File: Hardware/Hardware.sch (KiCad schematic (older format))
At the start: 18 parts, among them J1 Conn_01x02, J2 Conn_01x04, J4 Conn_01x02, J5 Conn_01x06, J6 Conn_01x08, J7 Conn_01x03, U1 ESP32-WROOM-32

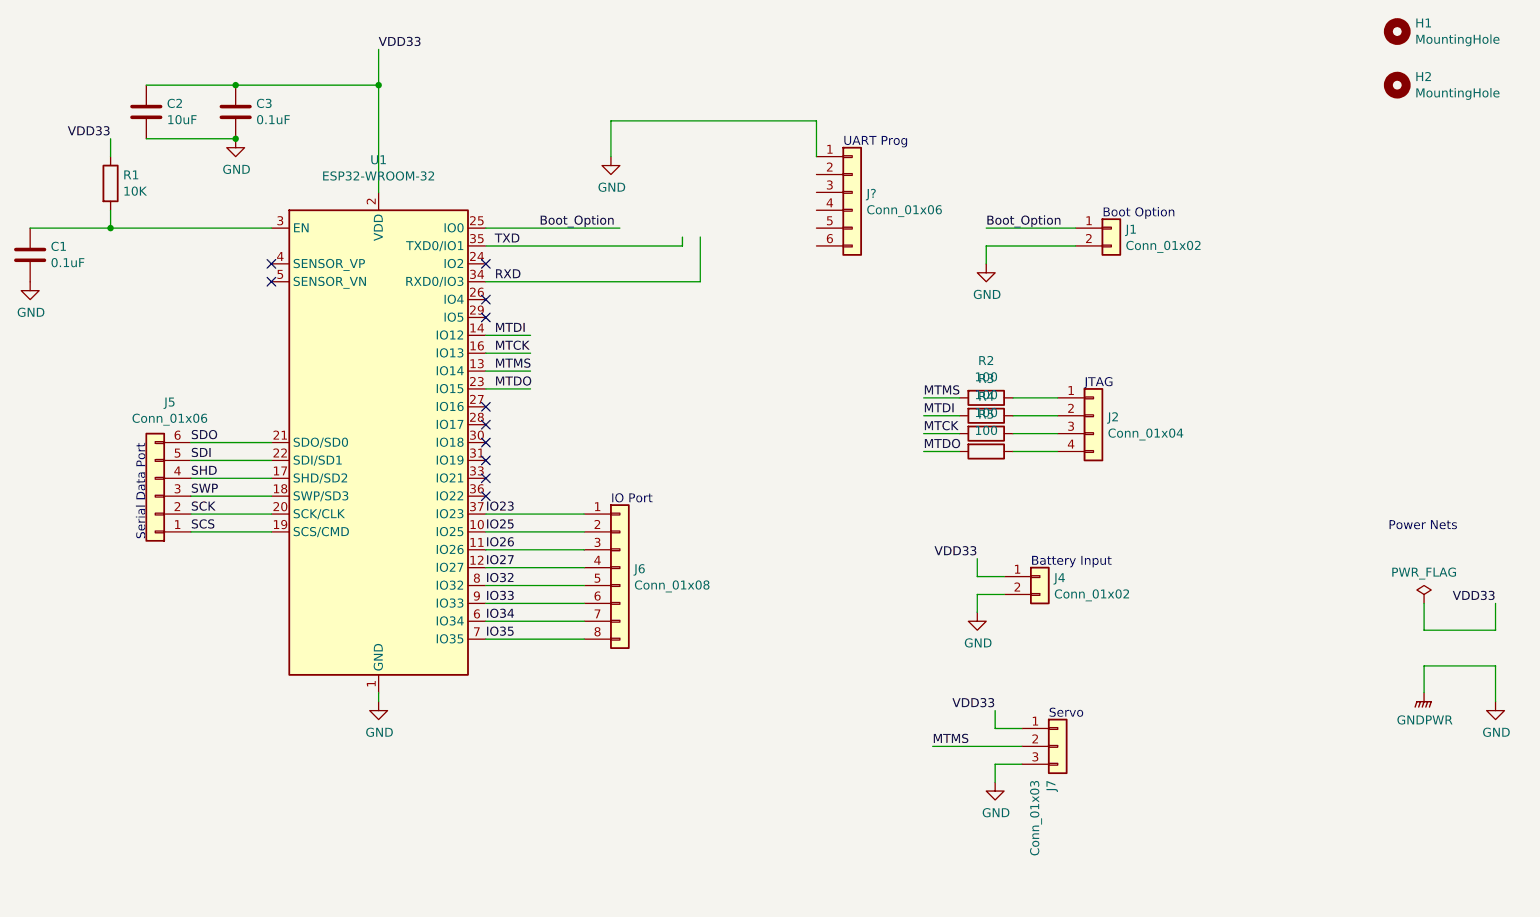
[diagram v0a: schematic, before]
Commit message: Programmer fix
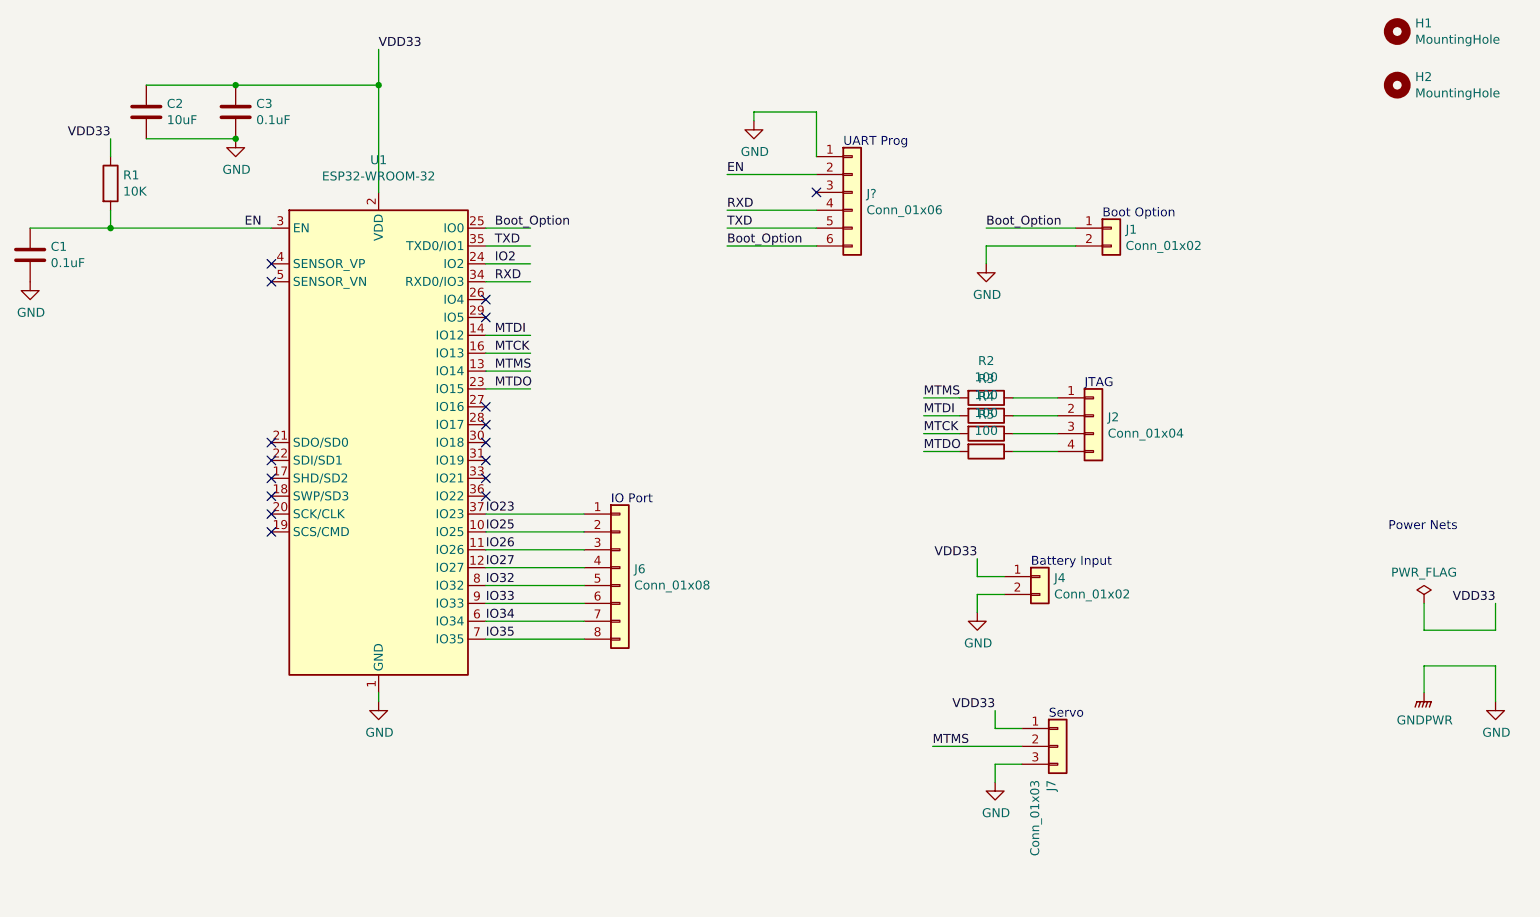
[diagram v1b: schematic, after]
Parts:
- removed J5: Conn_01x06, Connector_PinHeader_2.54mm:PinHeader_1x06_P2.54mm_Vertical, symbol Connector_Generic:Conn_01x06
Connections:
- net labels added: EN, IO2
- net labels removed: SCK, SCS, SDI, SDO, SHD, SWP
- wire segments 62 -> 59
- no-connect marks 11 -> 17
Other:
- note removed: "Serial Data Port"
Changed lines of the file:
@@
 	1    0    0    -1
 $EndComp
-Wire Wire Line
-	3200 2500 3950 2500
-Text Label 3500 2500 0    50   ~ 0
+Text Label 3250 2500 0    50   ~ 0
 Boot_Option
 $Comp
@@
 Wire Wire Line
 	6000 2600 6500 2600
-Wire Wire Line
-	3200 2600 4300 2600
-Wire Wire Line
-	4300 2600 4300 2550
-Wire Wire Line
-	4400 2550 4400 2800
-Wire Wire Line
-	4400 2800 3200 2800
-Text Notes 5200 2050 0    50   ~ 0
-UART Prog
 Text Label 3250 2600 0    50   ~ 0
 TXD
@@
 Text Label 3200 4800 0    50   ~ 0
 IO35
-$Comp
-L Connector_Generic:Conn_01x06 J5
-U 1 1 620D7FA6
-P 1350 4000
-F 0 "J5" H 1268 3475 50  0000 C CNN
-F 1 "Conn_01x06" H 1268 3566 50  0000 C CNN
-F 2 "Connector_PinHeader_2.54mm:PinHeader_1x06_P2.54mm_Vertical" H 1350 4000 50  0001 C CNN
-F 3 "~" H 1350 4000 50  0001 C CNN
-	1    1350 4000
-	-1   0    0    1
-$EndComp
-Wire Wire Line
-	2000 3800 1550 3800
-Wire Wire Line
-	1550 3900 2000 3900
-Wire Wire Line
-	1550 4000 2000 4000
-Wire Wire Line
-	1550 4100 2000 4100
-Wire Wire Line
-	2000 4200 1550 4200
-Wire Wire Line
-	1550 3700 2000 3700
-Text Label 1550 3700 0    50   ~ 0
-SDO
-Text Label 1550 3800 0    50   ~ 0
-SDI
-Text Label 1550 3900 0    50   ~ 0
-SHD
-Text Label 1550 4000 0    50   ~ 0
-SWP
-Text Label 1550 4100 0    50   ~ 0
-SCK
-Text Label 1550 4200 0    50   ~ 0
-SCS
-Text Notes 1300 4250 1    50   ~ 0
-Serial Data Port
-NoConn ~ 3200 2700
 NoConn ~ 3200 2900
 NoConn ~ 3200 3000
@@
 $EndComp
 $Comp
-L power:GND #PWR?
-U 1 1 6260035B
-P 3900 2100
-F 0 "#PWR?" H 3900 1850 50  0001 C CNN
-F 1 "GND" H 3905 1927 50  0000 C CNN
-F 2 "" H 3900 2100 50  0001 C CNN
-F 3 "" H 3900 2100 50  0001 C CNN
-	1    3900 2100
-	1    0    0    -1
-$EndComp
-Wire Wire Line
-	3900 2100 3900 1900
-Wire Wire Line
-	3900 1900 5050 1900
-Wire Wire Line
-	5050 1900 5050 2100
+L power:GND #PWR0105
+U 1 1 6209A315
+P 4700 1900
+F 0 "#PWR0105" H 4700 1650 50  0001 C CNN
+F 1 "GND" H 4705 1727 50  0000 C CNN
+F 2 "" H 4700 1900 50  0001 C CNN
+F 3 "" H 4700 1900 50  0001 C CNN
+	1    4700 1900
+	1    0    0    -1
+$EndComp
+Wire Wire Line
+	4700 1850 4700 1900
+Text Notes 5200 2050 0    50   ~ 0
+UART Prog
+Wire Wire Line
+	4700 1850 5050 1850
+Wire Wire Line
+	5050 1850 5050 2100
+Wire Wire Line
+	3200 2600 3450 2600
+Wire Wire Line
+	3200 2800 3450 2800
+Wire Wire Line
+	3200 2700 3450 2700
+NoConn ~ 2000 3700
+NoConn ~ 2000 3800
+NoConn ~ 2000 3900
+NoConn ~ 2000 4000
+NoConn ~ 2000 4100
+NoConn ~ 2000 4200
+Wire Wire Line
+	5050 2600 4550 2600
+Text Label 4550 2600 0    50   ~ 0
+Boot_Option
+Text Label 3250 2700 0    50   ~ 0
+IO2
+Text Label 1850 2500 0    50   ~ 0
+EN
+Wire Wire Line
+	3200 2500 3450 2500
+Wire Wire Line
+	5050 2200 4550 2200
+Wire Wire Line
+	5050 2400 4550 2400
+Wire Wire Line
+	5050 2500 4550 2500
+Text Label 4550 2200 0    50   ~ 0
+EN
+NoConn ~ 5050 2300
+Text Label 4550 2400 0    50   ~ 0
+RXD
+Text Label 4550 2500 0    50   ~ 0
+TXD
 $EndSCHEMATC

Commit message: layout reworking
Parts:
- removed J6: Conn_01x08, Connector_PinHeader_2.54mm:PinHeader_1x08_P2.54mm_Vertical, symbol Connector_Generic:Conn_01x08
- added D1: LED, LED_SMD:LED_0805_2012Metric_Castellated, symbol Device:LED
- J3: renamed from J?; footprint (none) -> Connector_PinHeader_2.54mm:PinHeader_1x06_P2.54mm_Vertical
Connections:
- wire segments 59 -> 60
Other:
- note removed: "IO Port"
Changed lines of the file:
@@
 Text Notes 6250 4400 0    50   ~ 0
 Battery Input
-$Comp
-L Connector_Generic:Conn_01x08 J6
-U 1 1 620BF760
-P 3950 4400
-F 0 "J6" H 4030 4392 50  0000 L CNN
-F 1 "Conn_01x08" H 4030 4301 50  0000 L CNN
-F 2 "Connector_PinHeader_2.54mm:PinHeader_1x08_P2.54mm_Vertical" H 3950 4400 50  0001 C CNN
-F 3 "~" H 3950 4400 50  0001 C CNN
-	1    3950 4400
-	1    0    0    -1
-$EndComp
-Wire Wire Line
-	3200 4800 3750 4800
-Wire Wire Line
-	3750 4700 3200 4700
-Wire Wire Line
-	3200 4600 3750 4600
-Wire Wire Line
-	3200 4500 3750 4500
-Wire Wire Line
-	3200 4400 3750 4400
-Wire Wire Line
-	3750 4300 3200 4300
-Wire Wire Line
-	3200 4200 3750 4200
-Wire Wire Line
-	3750 4100 3200 4100
-Text Notes 3900 4050 0    50   ~ 0
-IO Port
 Text Label 3200 4100 0    50   ~ 0
 IO23
@@
 $EndComp
 $Comp
-L Connector_Generic:Conn_01x06 J?
+L Connector_Generic:Conn_01x06 J3
 U 1 1 625FEE76
 P 5250 2300
-F 0 "J?" H 5330 2292 50  0000 L CNN
+F 0 "J3" H 5330 2292 50  0000 L CNN
 F 1 "Conn_01x06" H 5330 2201 50  0000 L CNN
-F 2 "" H 5250 2300 50  0001 C CNN
+F 2 "Connector_PinHeader_2.54mm:PinHeader_1x06_P2.54mm_Vertical" H 5250 2300 50  0001 C CNN
 F 3 "~" H 5250 2300 50  0001 C CNN
 	1    5250 2300
@@
 Text Label 4550 2500 0    50   ~ 0
 TXD
+Wire Wire Line
+	3750 4100 3200 4100
+Wire Wire Line
+	3200 4200 3750 4200
+Wire Wire Line
+	3750 4300 3200 4300
+Wire Wire Line
+	3200 4400 3750 4400
+Wire Wire Line
+	3200 4500 3750 4500
+Wire Wire Line
+	3750 4700 3200 4700
+Wire Wire Line
+	3200 4800 3750 4800
+$Comp
+L Device:LED D1
+U 1 1 6263E05E
+P 4050 4800
+F 0 "D1" V 4089 4682 50  0000 R CNN
+F 1 "LED" V 3998 4682 50  0000 R CNN
+F 2 "LED_SMD:LED_0805_2012Metric_Castellated" H 4050 4800 50  0001 C CNN
+F 3 "~" H 4050 4800 50  0001 C CNN
+	1    4050 4800
+	0    -1   -1   0
+$EndComp
+Wire Wire Line
+	4050 4600 4050 4650
+Wire Wire Line
+	3200 4600 4050 4600
+$Comp
+L power:GND #PWR0110
+U 1 1 62640CA7
+P 4050 4950
+F 0 "#PWR0110" H 4050 4700 50  0001 C CNN
+F 1 "GND" H 4055 4777 50  0000 C CNN
+F 2 "" H 4050 4950 50  0001 C CNN
+F 3 "" H 4050 4950 50  0001 C CNN
+	1    4050 4950
+	1    0    0    -1
+$EndComp
 $EndSCHEMATC

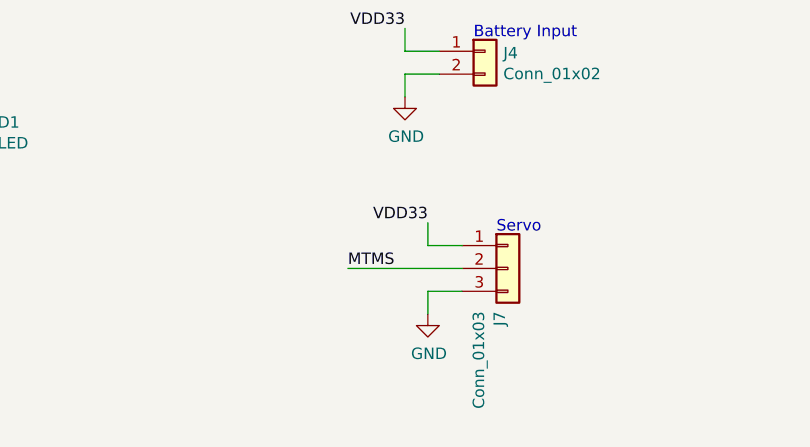
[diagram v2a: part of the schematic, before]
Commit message: Servo pin fix
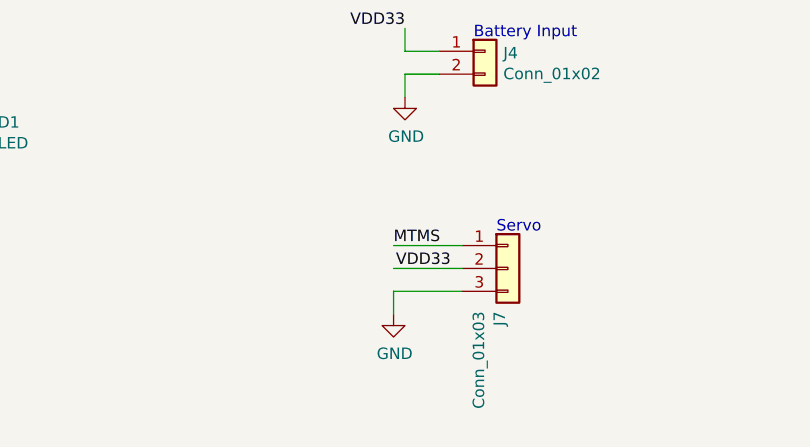
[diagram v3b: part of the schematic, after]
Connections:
- wire segments 60 -> 59
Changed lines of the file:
@@
 	1800 1700 2600 1700
 Connection ~ 1800 2000
-Text Label 5700 5400 0    50   ~ 0
+Text Label 5900 5300 0    50   ~ 0
 MTMS
-Wire Wire Line
-	5700 5400 6200 5400
 $Comp
-L Connector_Generic:Conn_01x03 J7
-U 1 1 6211C164
-P 6400 5400
-F 0 "J7" V 6364 5212 50  0000 R CNN
-F 1 "Conn_01x03" V 6273 5212 50  0000 R CNN
-F 2 "Connector_PinHeader_2.54mm:PinHeader_1x03_P2.54mm_Vertical" H 6400 5400 50  0001 C CNN
-F 3 "~" H 6400 5400 50  0001 C CNN
-	1    6400 5400
+L power:GND #PWR0109
+U 1 1 6211EACD
+P 5900 5600
+F 0 "#PWR0109" H 5900 5350 50  0001 C CNN
+F 1 "GND" H 5905 5427 50  0000 C CNN
+F 2 "" H 5900 5600 50  0001 C CNN
+F 3 "" H 5900 5600 50  0001 C CNN
+	1    5900 5600
 	1    0    0    -1
 $EndComp
 Wire Wire Line
-	6050 5300 6200 5300
-$Comp
-L power:GND #PWR0109
-U 1 1 6211EACD
-P 6050 5600
-F 0 "#PWR0109" H 6050 5350 50  0001 C CNN
-F 1 "GND" H 6055 5427 50  0000 C CNN
-F 2 "" H 6050 5600 50  0001 C CNN
-F 3 "" H 6050 5600 50  0001 C CNN
-	1    6050 5600
-	1    0    0    -1
-$EndComp
-Wire Wire Line
-	6200 5500 6050 5500
-Wire Wire Line
-	6050 5500 6050 5600
-Wire Wire Line
-	6050 5200 6050 5300
-Text Label 6050 5200 2    50   ~ 0
+	5900 5500 5900 5600
+Text Label 6150 5400 2    50   ~ 0
 VDD33
 Text Notes 6350 5250 0    50   ~ 0
@@
 	1    0    0    -1
 $EndComp
+Wire Wire Line
+	5900 5300 6200 5300
+Wire Wire Line
+	5900 5500 6200 5500
+Wire Wire Line
+	5900 5400 6200 5400
+$Comp
+L Connector_Generic:Conn_01x03 J7
+U 1 1 6211C164
+P 6400 5400
+F 0 "J7" V 6364 5212 50  0000 R CNN
+F 1 "Conn_01x03" V 6273 5212 50  0000 R CNN
+F 2 "Connector_PinHeader_2.54mm:PinHeader_1x03_P2.54mm_Vertical" H 6400 5400 50  0001 C CNN
+F 3 "~" H 6400 5400 50  0001 C CNN
+	1    6400 5400
+	1    0    0    -1
+$EndComp

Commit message: Voltage regulator & power drop testing
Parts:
- added U2: AMS1117-3.3, Package_TO_SOT_SMD:SOT-223-3_TabPin2, symbol Regulator_Linear:AMS1117-3.3
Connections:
- net labels added: PIR_INPUT
- wire segments 59 -> 63
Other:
- note added: "PIR Sensor\n"
- note removed: "Boot Option\n"
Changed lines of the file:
@@
 $EndComp
 Text Label 3250 2500 0    50   ~ 0
-Boot_Option
+PIR_INPUT
 $Comp
 L Connector_Generic:Conn_01x02 J1
@@
 $EndComp
 Text Notes 6650 2450 0    50   ~ 0
-Boot Option\n
+PIR Sensor\n
 Wire Wire Line
 	6000 2500 6500 2500
@@
 MTDO
 Text Label 6000 2500 0    50   ~ 0
-Boot_Option
+PIR_INPUT
 Wire Wire Line
 	6400 3650 6150 3650
@@
 Wire Wire Line
 	5950 4550 5950 4650
-Wire Wire Line
-	5950 4350 5950 4450
-Text Label 5950 4350 2    50   ~ 0
+Text Label 8000 4350 2    50   ~ 0
 VDD33
 Text Notes 6250 4400 0    50   ~ 0
@@
 	1    0    0    -1
 $EndComp
+$Comp
+L Regulator_Linear:AMS1117-3.3 U2
+U 1 1 62CE3E15
+P 7400 4350
+F 0 "U2" H 7400 4592 50  0000 C CNN
+F 1 "AMS1117-3.3" H 7400 4501 50  0000 C CNN
+F 2 "Package_TO_SOT_SMD:SOT-223-3_TabPin2" H 7400 4550 50  0001 C CNN
+F 3 "http://www.advanced-monolithic.com/pdf/ds1117.pdf" H 7500 4100 50  0001 C CNN
+	1    7400 4350
+	1    0    0    -1
+$EndComp
+Wire Wire Line
+	7700 4350 8000 4350
+Wire Wire Line
+	7100 4350 7000 4350
+Wire Wire Line
+	7000 4350 7000 4200
+Wire Wire Line
+	7000 4200 5950 4200
+Wire Wire Line
+	5950 4200 5950 4450
+$Comp
+L power:GND #PWR0111
+U 1 1 62CF0C97
+P 7400 4650
+F 0 "#PWR0111" H 7400 4400 50  0001 C CNN
+F 1 "GND" H 7405 4477 50  0000 C CNN
+F 2 "" H 7400 4650 50  0001 C CNN
+F 3 "" H 7400 4650 50  0001 C CNN
+	1    7400 4650
+	1    0    0    -1
+$EndComp

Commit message: Power supply fixes
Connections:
- net labels added: BATT_POS
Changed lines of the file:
@@
 $EndComp
 Text Label 8850 4600 2    50   ~ 0
-VDD33
+BATT_POS
 Wire Wire Line
 	8450 4600 8450 4750
@@
 	5900 5500 5900 5600
 Text Label 6150 5400 2    50   ~ 0
-VDD33
+BATT_POS
 Text Notes 6350 5250 0    50   ~ 0
 Servo
@@
 	1    0    0    -1
 $EndComp
+Text Label 5950 4200 0    50   ~ 0
+BATT_POS
 $EndSCHEMATC

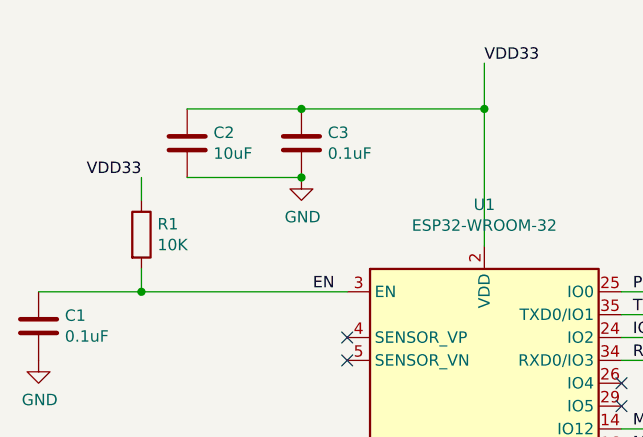
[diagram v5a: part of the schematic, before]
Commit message: Decoupling cap fix & servo power rewire
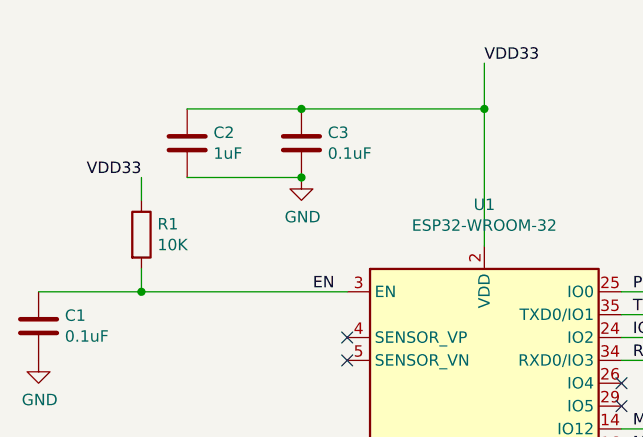
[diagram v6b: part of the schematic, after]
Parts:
- C2: value 10uF -> 1uF
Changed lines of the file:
@@
 P 1300 1850
 F 0 "C2" H 1415 1896 50  0000 L CNN
-F 1 "10uF" H 1415 1805 50  0000 L CNN
+F 1 "1uF" H 1415 1805 50  0000 L CNN
 F 2 "Capacitor_SMD:C_0805_2012Metric" H 1338 1700 50  0001 C CNN
 F 3 "~" H 1300 1850 50  0001 C CNN

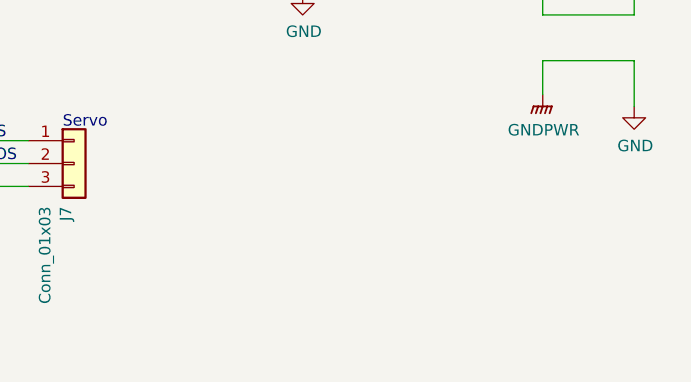
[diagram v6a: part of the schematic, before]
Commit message: Barrel jack was added to board
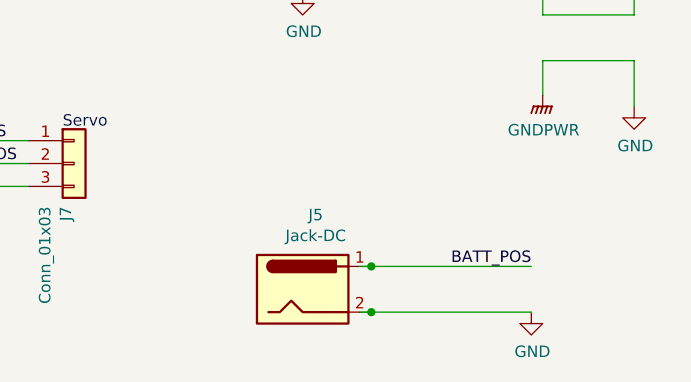
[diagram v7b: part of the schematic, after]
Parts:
- added J5: Jack-DC, Connector_BarrelJack:BarrelJack_CUI_PJ-102AH_Horizontal, symbol Connector:Jack-DC
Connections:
- wire segments 63 -> 67
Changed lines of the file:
@@
 Text Label 5950 4200 0    50   ~ 0
 BATT_POS
+Wire Wire Line
+	7650 5850 7700 5850
+Wire Wire Line
+	7650 6050 7700 6050
+Text Label 8400 5850 2    50   ~ 0
+BATT_POS
+$Comp
+L power:GND #PWR0112
+U 1 1 62E680F0
+P 8400 6050
+F 0 "#PWR0112" H 8400 5800 50  0001 C CNN
+F 1 "GND" H 8405 5877 50  0000 C CNN
+F 2 "" H 8400 6050 50  0001 C CNN
+F 3 "" H 8400 6050 50  0001 C CNN
+	1    8400 6050
+	1    0    0    -1
+$EndComp
+$Comp
+L Connector:Jack-DC J5
+U 1 1 62E6932D
+P 7400 5950
+F 0 "J5" H 7457 6275 50  0000 C CNN
+F 1 "Jack-DC" H 7457 6184 50  0000 C CNN
+F 2 "Connector_BarrelJack:BarrelJack_CUI_PJ-102AH_Horizontal" H 7450 5910 50  0001 C CNN
+F 3 "~" H 7450 5910 50  0001 C CNN
+	1    7400 5950
+	1    0    0    -1
+$EndComp
+Connection ~ 7700 5850
+Wire Wire Line
+	7700 5850 8400 5850
+Connection ~ 7700 6050
+Wire Wire Line
+	7700 6050 8400 6050
 $EndSCHEMATC
